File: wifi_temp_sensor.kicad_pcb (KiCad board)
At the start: 2 copper layers, 3 parts, among them IC1 ESP32-C3-WROOM-02-N4, J1 USB_C_Receptacle_USB2.0, J2 Batt_Conn

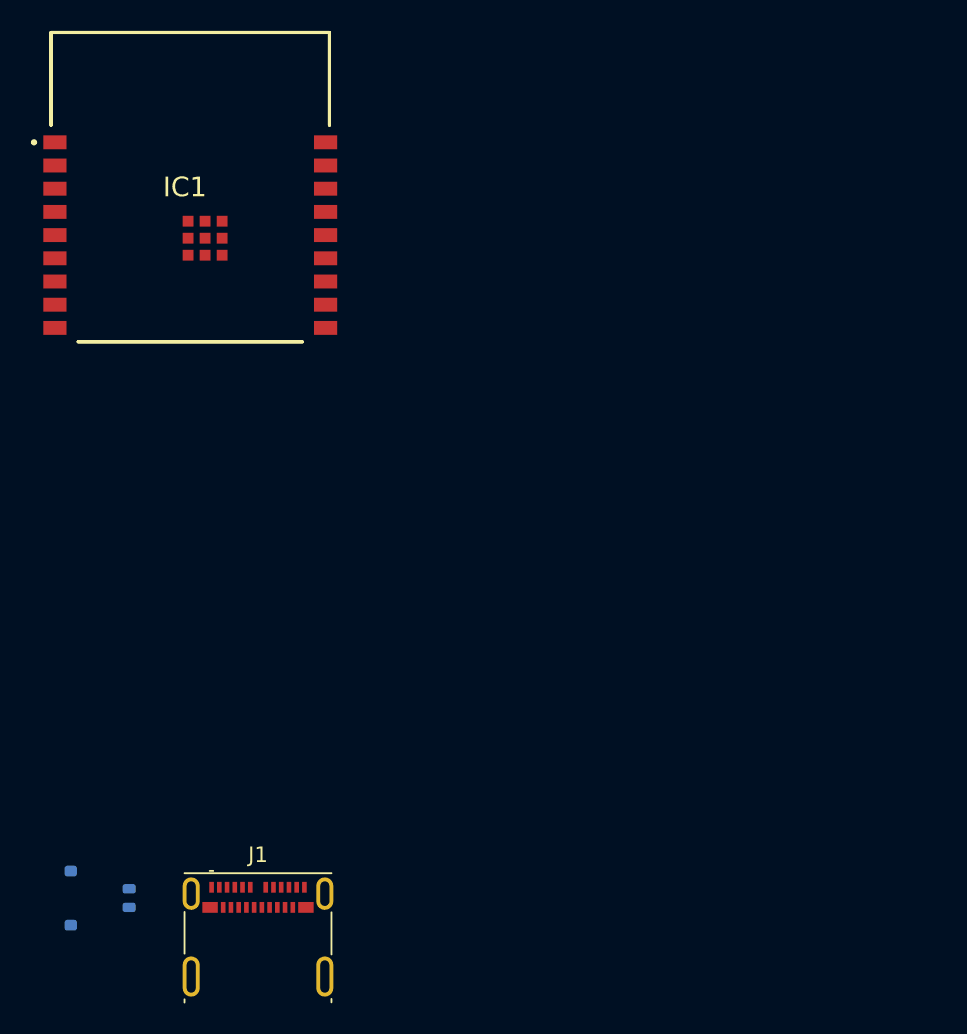
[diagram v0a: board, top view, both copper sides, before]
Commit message: Annotated and updated some of the PCB footprints
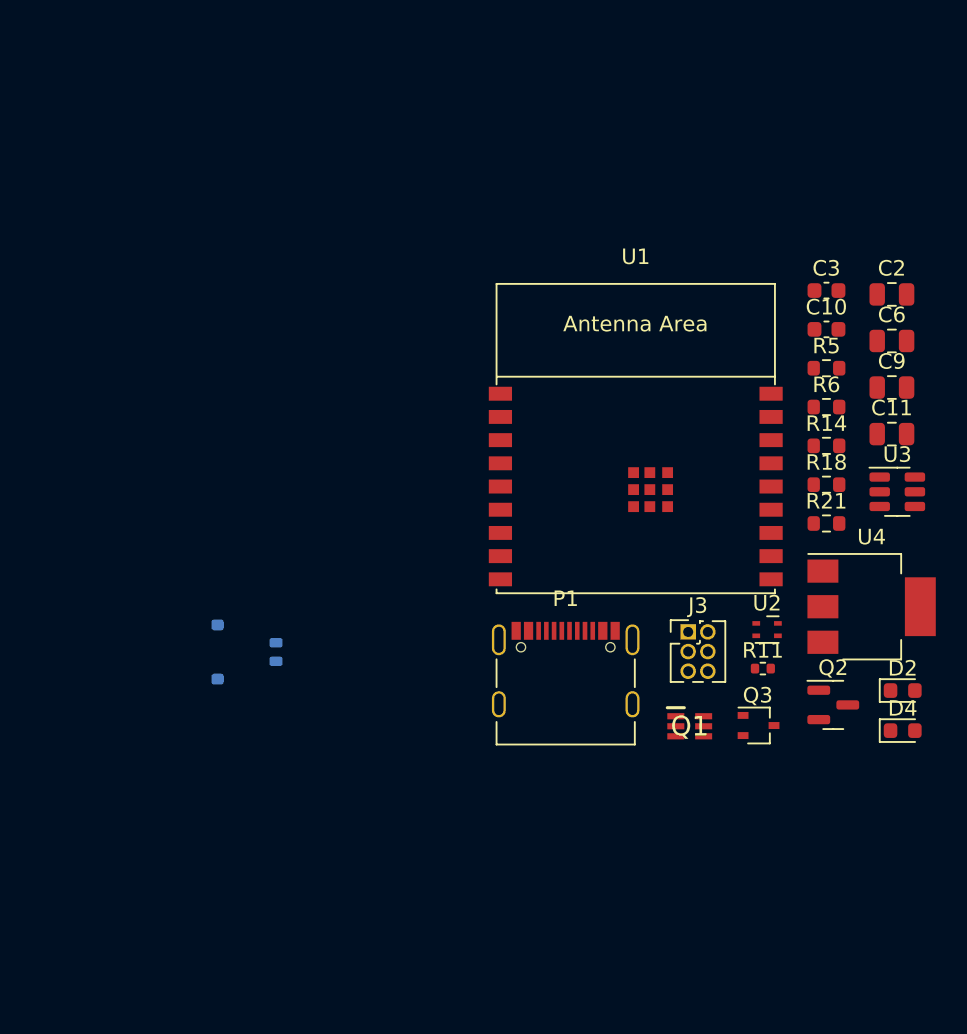
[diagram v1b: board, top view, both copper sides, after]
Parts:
- removed IC1: ESP32-C3-WROOM-02-N4, KiCad:ESP32C3WROOM02N4
- removed J1: USB_C_Receptacle_USB2.0, Connector_USB:USB_C_Receptacle_Molex_105450-0101
- added C10: 100nF, Capacitor_SMD:C_0603_1608Metric, F.Cu at (174.6, 73.1)
- added C11: 10uF, Capacitor_SMD:C_0805_2012Metric, F.Cu at (178.9, 79.9)
- added C2: 10uF, Capacitor_SMD:C_0805_2012Metric, F.Cu at (178.9, 70.9)
- added C3: 1uF, Capacitor_SMD:C_0603_1608Metric, F.Cu at (174.6, 70.6)
- added C6: 10uF, Capacitor_SMD:C_0805_2012Metric, F.Cu at (178.9, 73.9)
- added C9: 10uF, Capacitor_SMD:C_0805_2012Metric, F.Cu at (178.9, 76.9)
- added D2: LED_Small, LED_SMD:LED_0603_1608Metric, F.Cu at (179.6, 96.5)
- added D4: LED_Small, LED_SMD:LED_0603_1608Metric, F.Cu at (179.6, 99.1)
- added J3: Conn_02x03_Odd_Even, Connector_PinHeader_1.27mm:PinHeader_2x03_P1.27mm_Vertical, F.Cu at (165.7, 92.7)
- added P1: USB_C_Plug_USB2.0, Connector_USB:USB_C_Receptacle_Palconn_UTC16-G, F.Cu at (157.8, 95.1)
- added Q1: SSM6L09FUTE85LF, SamacSys_parts:SOT65P210X120-6N, F.Cu at (165.8, 98.8)
- added Q2: AO3401A, Package_TO_SOT_SMD:SOT-23, F.Cu at (175.1, 97.4)
- added Q3: BSS214NW, Package_TO_SOT_SMD:SOT-323_SC-70, F.Cu at (170.2, 98.7)
- added R11: 100K, Resistor_SMD:R_0402_1005Metric, F.Cu at (170.5, 95.0)
- added R14: 33R, Resistor_SMD:R_0603_1608Metric, F.Cu at (174.6, 80.7)
- added R18: 10K, Resistor_SMD:R_0603_1608Metric, F.Cu at (174.6, 83.2)
- added R21: 33R, Resistor_SMD:R_0603_1608Metric, F.Cu at (174.6, 85.7)
- added R5: 10K, Resistor_SMD:R_0603_1608Metric, F.Cu at (174.6, 75.6)
- added R6: 1K, Resistor_SMD:R_0603_1608Metric, F.Cu at (174.6, 78.1)
- added U1: ESP32-C3-WROOM-02, PCM_Espressif:ESP32-C3-WROOM-02, F.Cu at (162.3, 83.2)
- added U2: SHT4x, Sensor_Humidity:Sensirion_DFN-4_1.5x1.5mm_P0.8mm_SHT4x_NoCentralPad, F.Cu at (170.8, 92.5)
- added U3: WE-TVS-82400102, Package_TO_SOT_SMD:SOT-23-6, F.Cu at (179.2, 83.6)
- added U4: LD1117S33TR_SOT223, Package_TO_SOT_SMD:SOT-223-3_TabPin2, F.Cu at (177.5, 91.0)
- moved J2 18.5 mm to (137.2, 94.0)
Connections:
- net V_BAT renamed Net-(J2-Pin_2)

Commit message: Notes and initial PCB layout
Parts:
- added C1: 1uF, Capacitor_SMD:C_0603_1608Metric, F.Cu at (271.7, 76.0)
- added C12: 100nF, Capacitor_SMD:C_0603_1608Metric, B.Cu at (207.3, 110.9)
- added C4: 100nF, Capacitor_SMD:C_0603_1608Metric, F.Cu at (218.2, 89.5)
- added C5: 100nF, Capacitor_SMD:C_0603_1608Metric, F.Cu at (226.2, 41.8)
- added C7: 22pF, Capacitor_SMD:C_0603_1608Metric, F.Cu at (164.7, 97.2)
- added C8: 22pF, Capacitor_SMD:C_0603_1608Metric, F.Cu at (164.7, 100.5)
- added D1: D_Schottky, Diode_SMD:D_0603_1608Metric, F.Cu at (254.2, 82.0)
- added F1: Polyfuse_Small, Fuse:Fuse_0603_1608Metric, F.Cu at (183.2, 95.2)
- added IC2: BQ21040DBVR, TI BQ21040:SOT95P280X145-6N, B.Cu at (208.5, 94.5)
- added R1: 100K, Resistor_SMD:R_0603_1608Metric, F.Cu at (222.2, 92.0)
- added R10: 10k, Resistor_SMD:R_0603_1608Metric, F.Cu at (171.2, 54.0)
- added R12: 5.1K, Resistor_SMD:R_0603_1608Metric, F.Cu at (174.2, 100.2)
- added R13: 5.1K, Resistor_SMD:R_0603_1608Metric, F.Cu at (169.7, 100.5)
- added R15: 10k, Resistor_SMD:R_0603_1608Metric, F.Cu at (175.2, 49.0)
- added R16: 10k, Resistor_SMD:R_0603_1608Metric, F.Cu at (175.2, 51.5)
- added R17: 10R, Resistor_SMD:R_0603_1608Metric, F.Cu at (141.1, 67.2)
- added R19: 33K, Resistor_SMD:R_0603_1608Metric, B.Cu at (207.3, 120.5)
- added R2: 100K, Resistor_SMD:R_0603_1608Metric, F.Cu at (222.2, 94.5)
- added R20: 10K, Resistor_SMD:R_0603_1608Metric, B.Cu at (207.3, 122.8)
- added R3: 10k, Resistor_SMD:R_0603_1608Metric, F.Cu at (221.0, 37.2)
- added R4: 10k, Resistor_SMD:R_0603_1608Metric, F.Cu at (220.9, 35.2)
- added R9: R_Small, Resistor_SMD:R_0603_1608Metric, B.Cu at (207.3, 115.5)
- added SW1: SW_SPST, Button_Switch_SMD:SW_SPDT_CK-JS102011SAQN, B.Cu at (219.3, 103.8)
- C3, C6, Q1, R18: moved to B.Cu
- moved C2 93.2 mm to (271.6, 79.4)
- moved U4 84.7 mm to (261.5, 79.8)
- moved U2 79.4 mm to (226.5, 36.0), turned to -90 degrees
- moved J2 71.5 mm to (208.2, 102.0)
- moved Q2 71.4 mm to (245.0, 82.8)
- moved J3 68.1 mm to (212.7, 43.5)
- moved R5 66.6 mm to (241.1, 79.5)
- moved R6 66.6 mm to (241.1, 82.0)
- moved R11 64.1 mm to (106.7, 88.3)
- moved D4 57.3 mm to (177.8, 41.8)
- moved U1 53.8 mm to (197.2, 42.2)
- moved C3 53.7 mm to (207.3, 113.2), turned to 180 degrees
- moved R18 53.2 mm to (207.3, 125.1), turned to 180 degrees
- moved C6 52.5 mm to (207.3, 118.0), turned to 180 degrees
- moved Q1 52.4 mm to (218.0, 95.0), turned to 180 degrees
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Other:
- board outline added: 50 x 77 mm
- board text added: "I've seen designs with a separated section of the PCB for the sensor (AHT20) What do you think?"
